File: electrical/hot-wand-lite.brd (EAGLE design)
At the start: 112 x 72 mm, 79 parts, among them IC1 12V R-78K12-2.0, IC2 AMS1117-5.0, Q1 NCHAN, Q2 SIRS5800DP-T1-GE3, Q3 DMTH64M2LPDWQ-13, Q4 2N7002K, U1 SEEED-XIAO-SAMD21, U2 1EDN8511BXUSA1, U3 LM74700QDBVTQ1, U4 AP53781

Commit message: missed a route
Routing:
- net +24V: track 50.0 -> 54.0 mm
- net N$12: vias 0 -> 2
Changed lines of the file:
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@@
 <wire x1="50" y1="53.96" x2="53.28" y2="53.96" width="1.5" layer="1"/>
 <wire x1="53.28" y1="53.96" x2="59.2" y2="48.04" width="1.5" layer="1"/>
-<wire x1="45.96" y1="53.96" x2="46" y2="53.95" width="0" layer="19" extent="1-16"/>
+<wire x1="46" y1="53.95" x2="50" y2="53.95" width="1" layer="16"/>
+<wire x1="50" y1="53.95" x2="50" y2="53.96" width="1" layer="16"/>
 </signal>
 <signal name="N$14">
@@
 <wire x1="110.3" y1="31.2" x2="110.3" y2="33.175" width="1" layer="16"/>
 <wire x1="110.3" y1="33.175" x2="109.6" y2="33.175" width="1" layer="16"/>
-<wire x1="108.4" y1="40.8" x2="108.4" y2="40.8" width="0" layer="19" extent="1-16"/>
-<wire x1="109.6" y1="33.175" x2="109.6" y2="33.175" width="0" layer="19" extent="1-16"/>
+<via x="108.4" y="40.8" extent="1-16" drill="0.3" shape="octagon"/>
+<via x="110.3" y="31.2" extent="1-16" drill="0.3" shape="octagon"/>
 </signal>
 </signals>

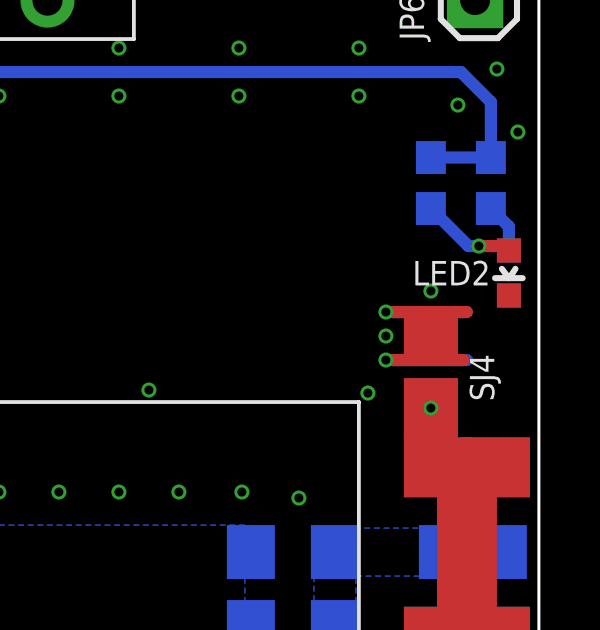
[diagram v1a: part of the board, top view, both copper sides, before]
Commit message: lite, moved LED, updated inductor comments
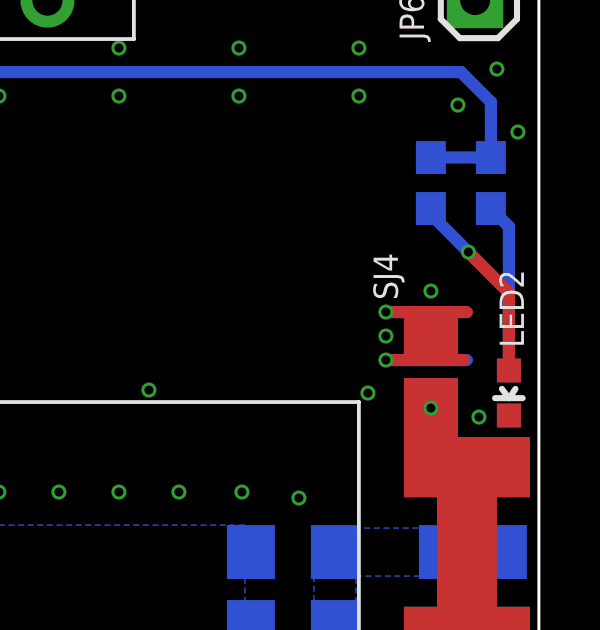
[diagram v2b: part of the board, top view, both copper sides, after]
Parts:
- moved LED1 4.00 mm to (111.0, 41.3)
- moved LED2 4.00 mm to (111.0, 41.3)
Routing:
- net N$46: track 1.65 -> 5.65 mm
- net N$8: track 3.27 -> 6.47 mm
- net GND: vias 333 -> 334
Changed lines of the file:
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@@
 <attribute name="JLCPARTNUM" value="C2453886" x="33" y="56" size="1.778" layer="27" display="off"/>
 </element>
-<element name="LED1" library="hot-wand" package="LED-0603" value="LED" x="111" y="45.3" smashed="yes" rot="MR180">
-<attribute name="JLC-DNP" value="1" x="111" y="45.3" size="1.778" layer="28" rot="MR180" display="off"/>
-<attribute name="NAME" x="110.189" y="44.9985" size="0.8128" layer="26" font="fixed" rot="MR0"/>
+<element name="LED1" library="hot-wand" package="LED-0603" value="LED" x="111" y="41.3" smashed="yes" rot="MR180">
+<attribute name="JLC-DNP" value="1" x="111" y="41.3" size="1.778" layer="28" rot="MR180" display="off"/>
+<attribute name="NAME" x="110.5985" y="42.811" size="0.8128" layer="26" font="fixed" rot="MR90"/>
 </element>
 <element name="PCB1" library="hot-wand" package="PCB-OUTLINE" value="PCB-OUTLINE" x="0" y="0" smashed="yes">
@@
 <attribute name="VALUE" x="108.843" y="49.716" size="0.8128" layer="28" font="vector" rot="MR270"/>
 </element>
-<element name="LED2" library="hot-wand" package="LED-0603" value="LED" x="111" y="45.3" smashed="yes" rot="R180">
-<attribute name="JLC-DNP" value="1" x="111" y="45.3" size="1.778" layer="27" rot="R180" display="off"/>
-<attribute name="NAME" x="110.389" y="45.7015" size="0.8128" layer="25" font="fixed" rot="R180"/>
+<element name="LED2" library="hot-wand" package="LED-0603" value="LED" x="111" y="41.3" smashed="yes" rot="R180">
+<attribute name="JLC-DNP" value="1" x="111" y="41.3" size="1.778" layer="27" rot="R180" display="off"/>
+<attribute name="NAME" x="111.5015" y="42.811" size="0.8128" layer="25" font="fixed" rot="R90"/>
 </element>
 <element name="PCB2" library="hot-wand" package="PCB-ART-VERSION-LITE" value="PCB-ART-VER-LITE" x="41.5" y="5.1" smashed="yes" rot="MR0">
@@
 </element>
 <element name="SJ4" library="hot-wand" package="1206-SJ" value="SJ-SMALL-1206-SJ" x="108.4" y="42" smashed="yes" rot="R90">
-<attribute name="NAME" x="109.7" y="42.6" size="0.8128" layer="25" font="fixed" rot="R270"/>
+<attribute name="NAME" x="107.3" y="44.4" size="0.8128" layer="25" font="fixed" rot="R90"/>
 </element>
 <element name="SJ5" library="hot-wand" package="1206-SJ" value="SJ-SMALL-1206-SJ" x="108.4" y="42" smashed="yes" rot="MR90">
@@
 <contactref element="IC2" pad="1"/>
 <contactref element="U1" pad="13"/>
-<wire x1="111" y1="44.6" x2="111" y2="44.55" width="0.4064" layer="16"/>
+<wire x1="111" y1="40.6" x2="111" y2="40.55" width="0.4064" layer="16"/>
 <contactref element="LED2" pad="C"/>
 <via x="26.8" y="37.3" extent="1-16" drill="0.3" shape="octagon"/>
@@
 <via x="108.8" y="28.8" extent="1-16" drill="0.3" shape="octagon"/>
 <via x="108.8" y="29.6" extent="1-16" drill="0.3" shape="octagon"/>
+<via x="110" y="40.5" extent="1-16" drill="0.3" shape="octagon"/>
 </signal>
 <signal name="+24V">
@@
 <contactref element="R5" pad="2"/>
 <contactref element="LED1" pad="A"/>
-<wire x1="111" y1="46.05" x2="111" y2="46.85" width="0.4064" layer="16"/>
+<wire x1="111" y1="42.05" x2="111" y2="46.85" width="0.4064" layer="16"/>
 <wire x1="111" y1="46.85" x2="110.4" y2="47.45" width="0.4064" layer="16"/>
 </signal>
@@
 <contactref element="LED2" pad="A"/>
 <contactref element="R6" pad="2"/>
-<wire x1="108.4" y1="47.45" x2="109.65" y2="46.2" width="0.4064" layer="16"/>
-<wire x1="109.65" y1="46.2" x2="110" y2="46.2" width="0.4064" layer="16"/>
-<via x="110" y="46.2" extent="1-16" drill="0.3" shape="octagon"/>
-<wire x1="110" y1="46.2" x2="111" y2="46.2" width="0.4064" layer="1"/>
-<wire x1="111" y1="46.2" x2="111" y2="46.05" width="0.4064" layer="1"/>
+<wire x1="108.4" y1="47.45" x2="108.4" y2="47.26" width="0.4064" layer="16"/>
+<wire x1="108.4" y1="47.26" x2="109.65" y2="46" width="0.4064" layer="16"/>
+<via x="109.65" y="46" extent="1-16" drill="0.3" shape="octagon"/>
+<wire x1="109.65" y1="46" x2="111" y2="44.65" width="0.4064" layer="1"/>
+<wire x1="111" y1="44.65" x2="111" y2="42.05" width="0.4064" layer="1"/>
 </signal>
 <signal name="ADC">

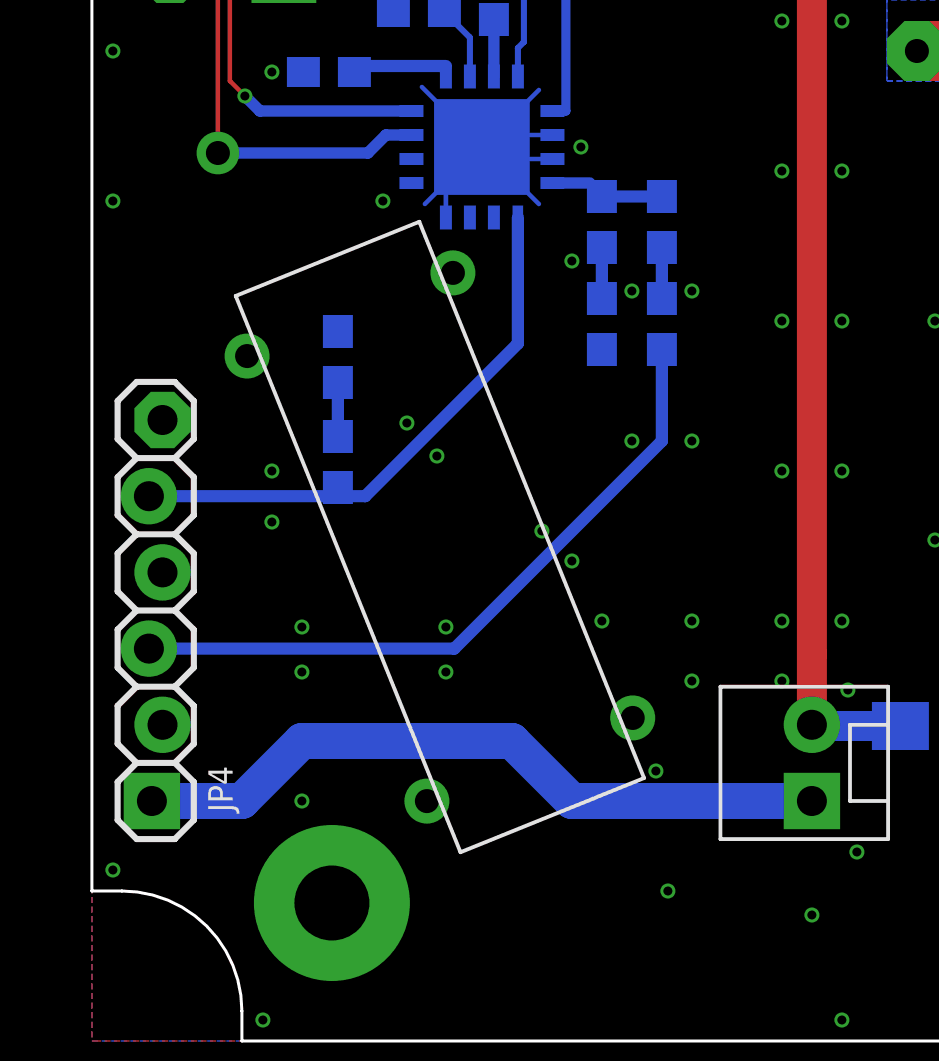
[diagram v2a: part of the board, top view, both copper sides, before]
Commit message: added selector for 28V
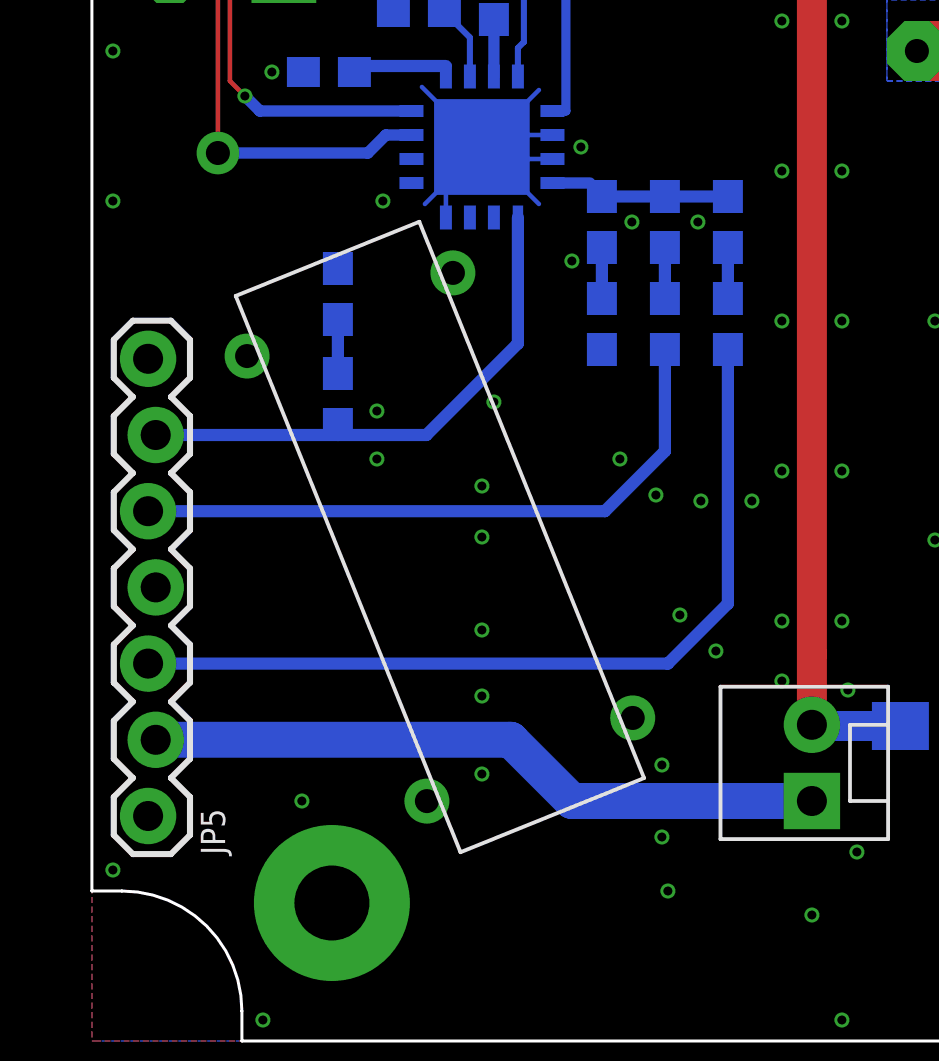
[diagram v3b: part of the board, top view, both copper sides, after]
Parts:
- removed JP4: (no value), hot-wand:1X06_LOCK
- added JP5: (no value), hot-wand:1X07_LOCK
- added R21: 4K7, hot-wand:0603-RES
- added R22: 470Ω, hot-wand:0603-RES
- R19: value 4K7 -> 51K
- R20: value 470Ω -> 1K
- moved R20 51.9 mm to (19.1, 23.9), turned to 270 degrees
- moved R19 49.3 mm to (19.1, 27.3), turned to 270 degrees
- moved R17 2.20 mm to (21.2, 27.3)
- moved R18 2.20 mm to (21.2, 23.9)
- moved R13 2.10 mm to (8.20, 21.4)
- moved R14 2.10 mm to (8.20, 24.9)
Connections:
- removed net USB-V-SEL: JP4.3, R18.2
- new net N$13: R19.2, R20.1
- new net USB-V-SEL-20V: JP5.3, R18.2
- new net USB-V-SEL-28V: JP5.5, R20.2
- net +24V: now also R21.2; no longer R19.2
- net ADC: now also R21.1, R22.1; no longer R19.1, R20.1
- net FAN-CTRL: now also JP5.2; no longer JP4.1
- net GND: now also JP5.1, JP5.4, JP5.7, R22.2; no longer JP4.2, JP4.4, JP4.6, R20.2
- net N$42: now also R19.1
- net USB-I-SEL: now also JP5.6; no longer JP4.5
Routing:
- net USB-V-SEL-20V: track 0.00 -> 28.6 mm
- net USB-V-SEL: track 23.0 -> 0.00 mm
- net USB-V-SEL-28V: track 0.00 -> 21.4 mm
- net N$42: track 3.85 -> 6.05 mm
- net N$13: track 0.00 -> 1.70 mm
- net USB-I-SEL: track 18.9 -> 17.9 mm
- net FAN-CTRL: track 23.7 -> 22.7 mm

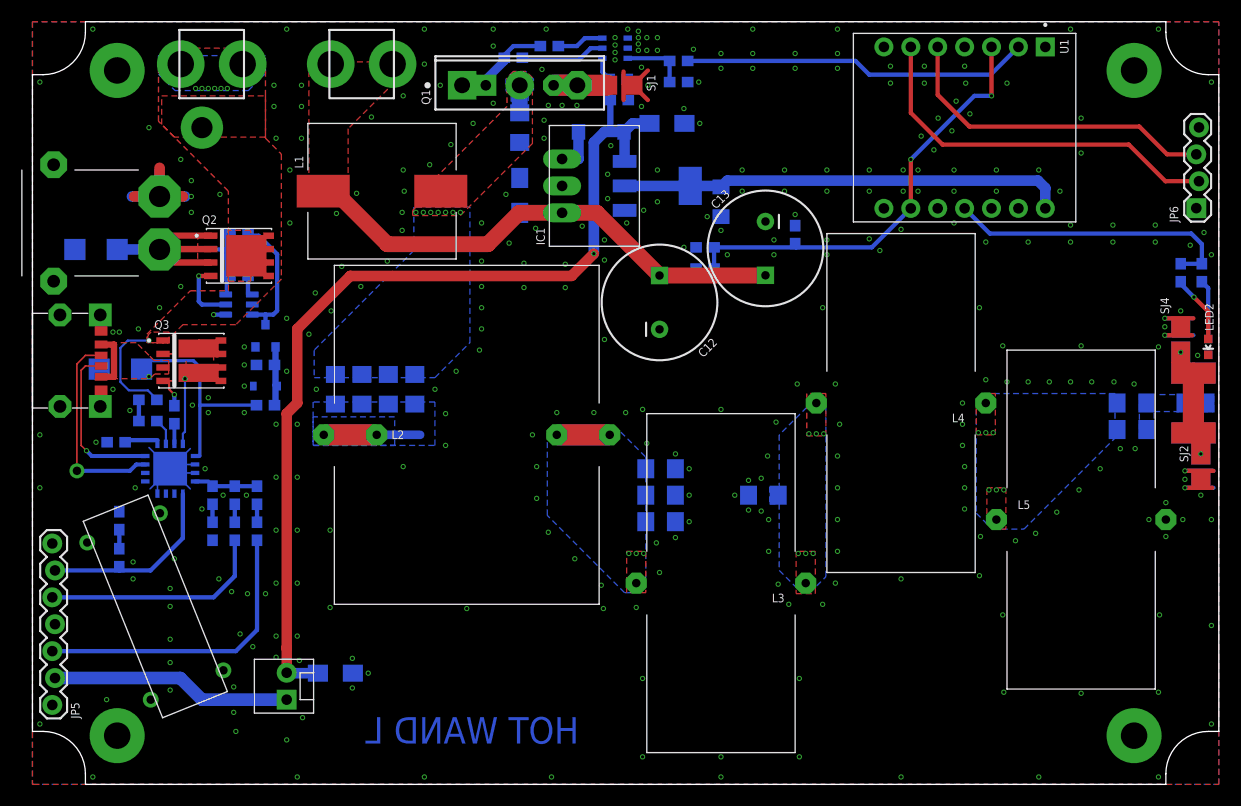
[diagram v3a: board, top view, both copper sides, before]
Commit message: changing lite pcb to match mosfet changes to other design
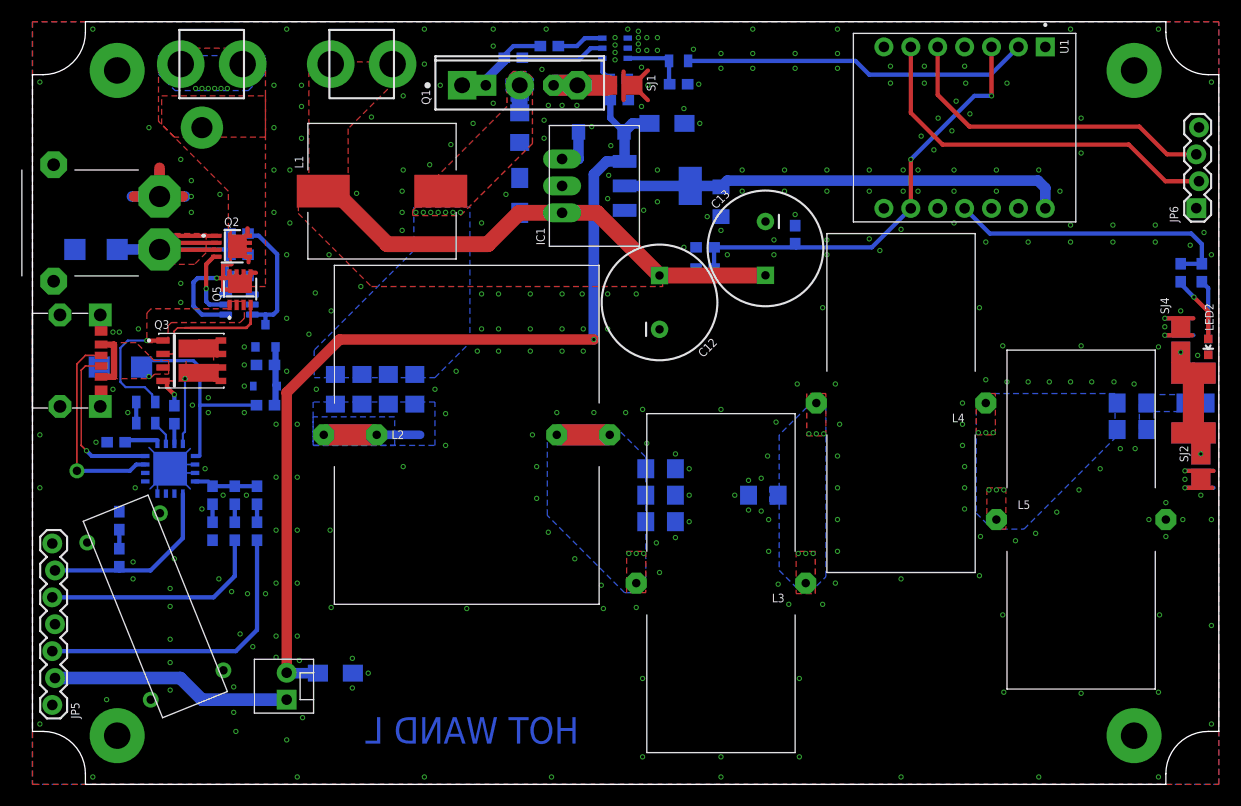
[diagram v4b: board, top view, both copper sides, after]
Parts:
- added Q5: SIS862ADN-T1-GE3, hot-wand:POWERPAK-1212-8
- Q2: value SIRS5800DP-T1-GE3 -> SIS862ADN-T1-GE3; device hot-wand:POWERPAK-SO8-X1 -> hot-wand:POWERPAK-1212-8
- R1, R10, R11: device hot-wand:0603-RES -> hot-wand:0805
- moved Q2 1.14 mm to (18.8, 50.8)
- moved R10 0.28 mm to (10.7, 34.1)
- moved R11 0.28 mm to (10.7, 36.1)
- moved R2 0.20 mm to (61.0, 66.1)
- moved TVS2 0.20 mm to (8.30, 39.4)
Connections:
- new net N$16: Q3.1, Q5.1, Q5.2, Q5.3, R11.1
- net DC-SRC: now also Q5.5, Q5.6, Q5.7, Q5.8, Q5.9; no longer Q3.1, R11.1
- net N$37: now also Q5.4
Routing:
- net N$16: track 0.00 -> 12.0 mm, vias 0 -> 1
- net N$37: track 7.03 -> 18.6 mm
- net DC-SRC: track 11.5 -> 18.6 mm, vias 9 -> 8
- net N$31: track 32.8 -> 35.2 mm
- net +12V: track 94.1 -> 92.9 mm
- net N$29: track 6.20 -> 6.73 mm
- net GND: vias 334 -> 337
- added copper zone on layer 1, net N$16
